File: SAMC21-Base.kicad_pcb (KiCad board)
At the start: 4 copper layers, 25.4 x 42.5 mm, 52 parts, among them J1 Conn_01x04, J2 Conn_01x10, J3 Conn_01x10, J5 Conn_ARM_JTAG_SWD_10, U1 ATSAMC21E18A-AUT, U2 TJA1043T, U3 TPS560430Y, U4 MCP1703A, Y1 ABM3-8.000MHZ-D2Y-T

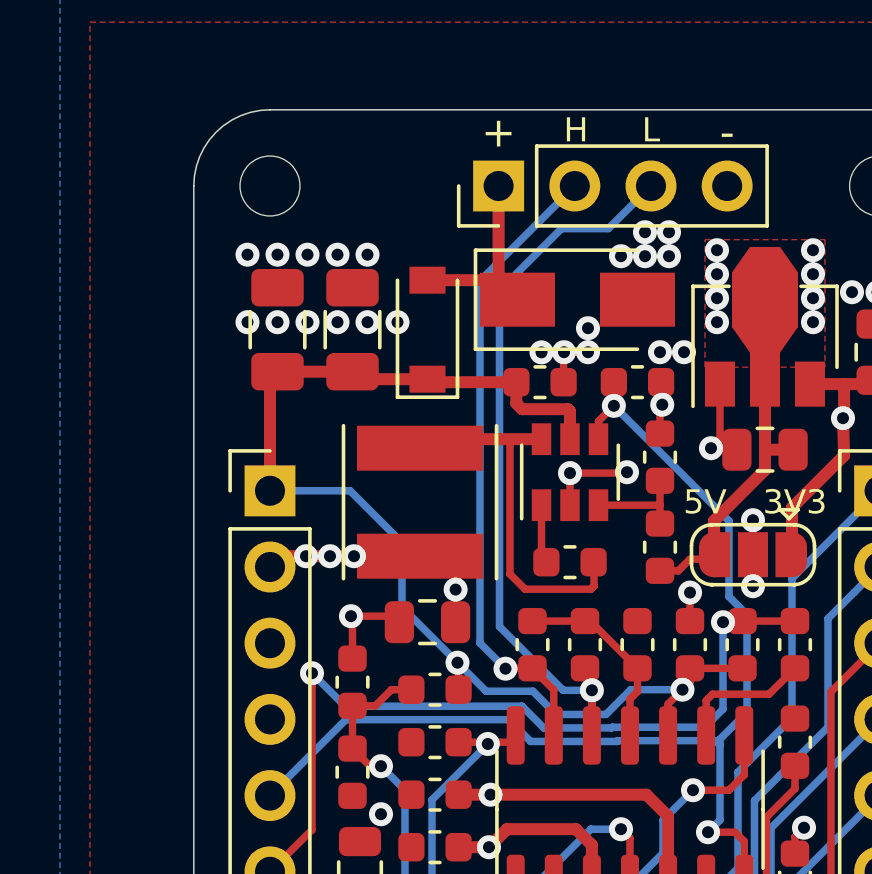
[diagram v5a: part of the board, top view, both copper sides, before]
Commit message: add various ESD, EMV and overcurrent protections
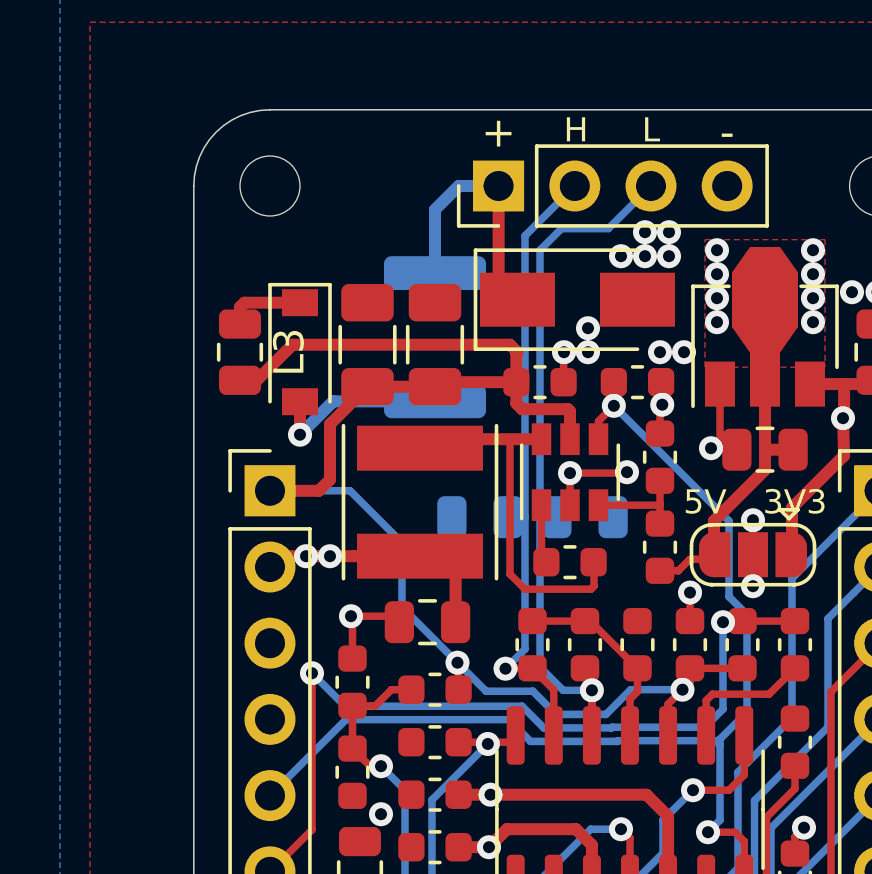
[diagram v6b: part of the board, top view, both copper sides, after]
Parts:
- added F1: 1812L020/60, Fuse:Fuse_1812_4532Metric, B.Cu at (107.1, 58.4)
- added L3: MLP2012V4R7MT0S1, Inductor_SMD:L_0805_2012Metric, F.Cu at (100.6, 58.9)
- added RV1: CT0805K25G, Resistor_SMD:R_0805_2012Metric, B.Cu at (108.6, 64.4)
- added RV2: CT0805K25G, Resistor_SMD:R_0805_2012Metric, B.Cu at (112.1, 64.4)
- moved D1 4.32 mm to (102.6, 58.9), turned to 270 degrees
- moved C20 3.04 mm to (104.8, 58.6)
- moved C1 2.80 mm to (107.1, 58.6)
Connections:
- D1 pad 1: +36V -> Net-(D1-Pad1)
- D1 pad 2: VBUS -> Net-(D1-Pad2)
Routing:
- net +36V: track 39.4 -> 48.8 mm
- net Net-(D1-Pad2): track 0.00 -> 6.06 mm, vias 0 -> 1
- net Net-(D1-Pad1): track 0.00 -> 2.62 mm
- net VBUS: track 5.54 -> 7.72 mm
- net GND: track 30.5 -> 29.8 mm, vias 40 -> 28
- net CAN_L: track 25.5 -> 24.9 mm
- net +5V: track 44.2 -> 44.0 mm, vias 13 -> 11

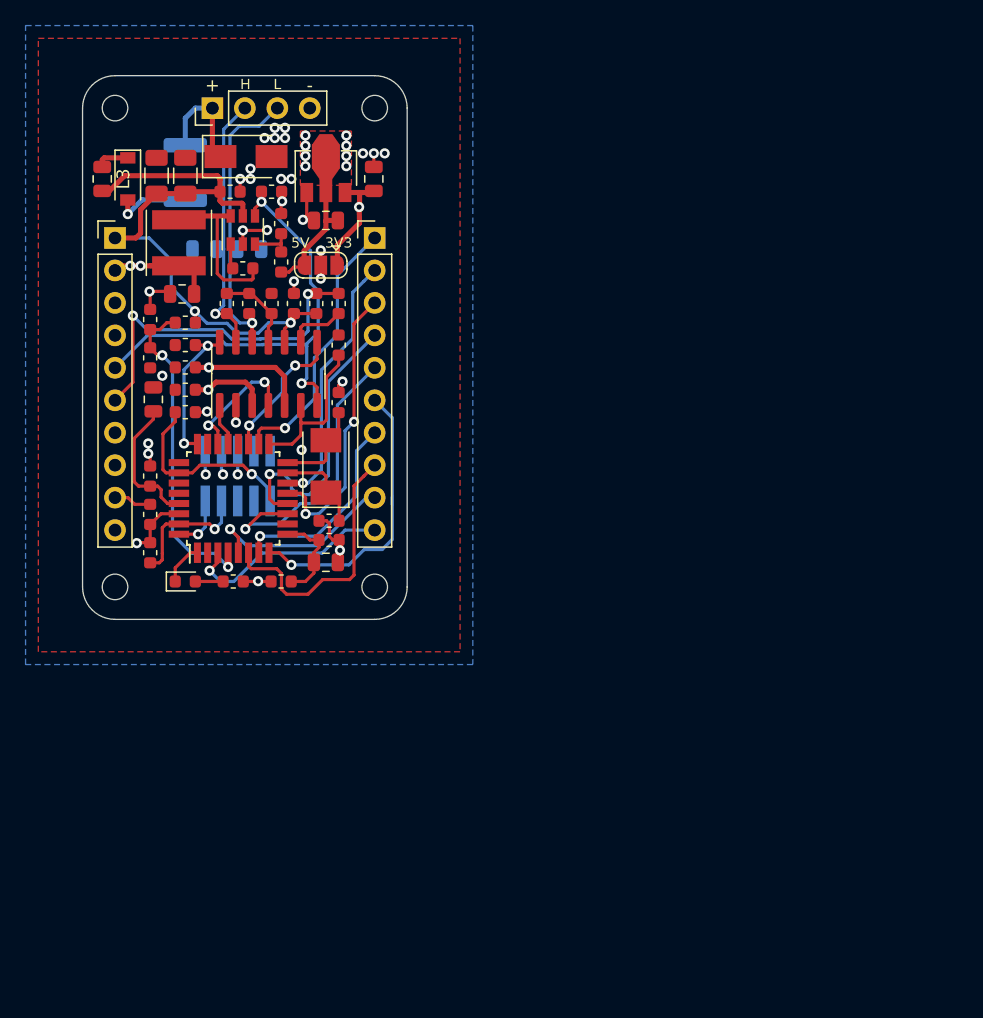
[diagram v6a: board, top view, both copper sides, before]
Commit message: redo layout. from scratch.
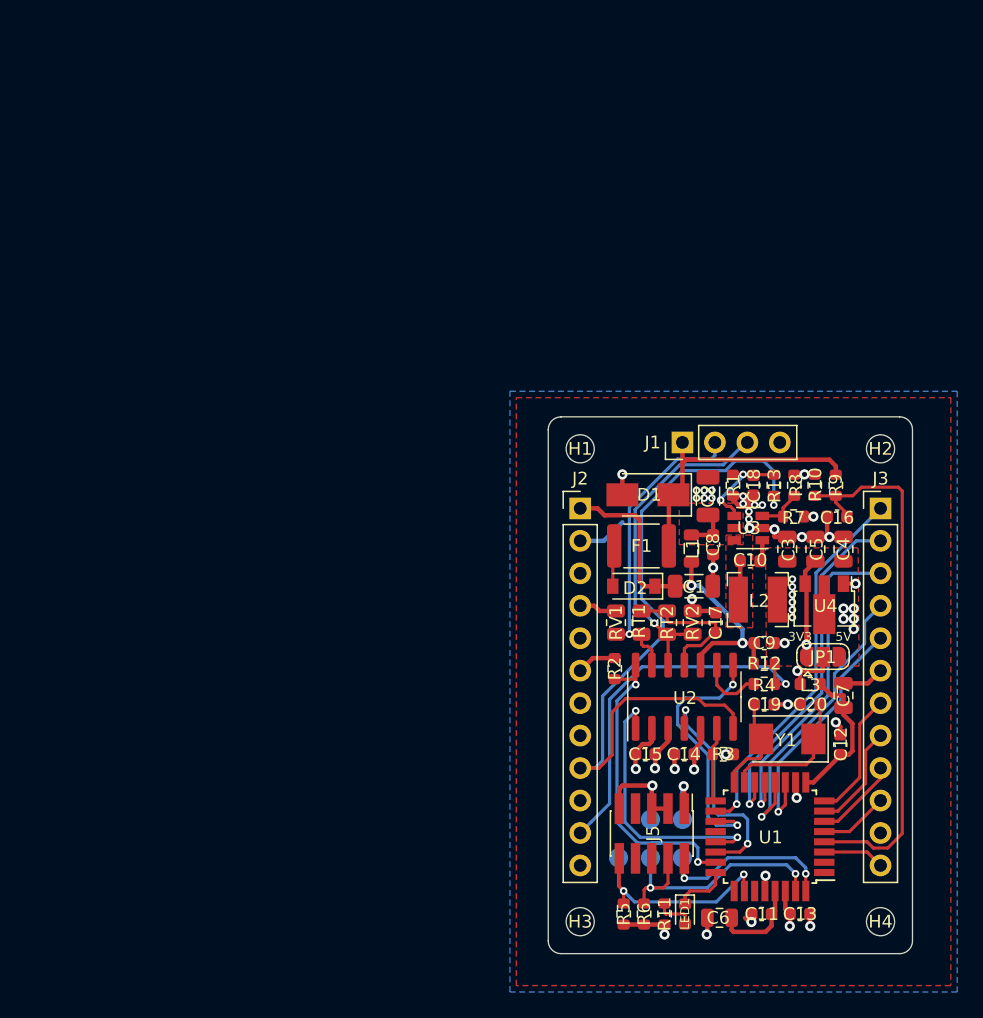
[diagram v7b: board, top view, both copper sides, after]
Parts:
- removed D3: SMAJ40A, Diode_SMD:D_SMA
- added C4: 10uF/10V, Capacitor_SMD:C_0805_2012Metric, F.Cu at (158.6, 87.8)
- added LED1: LED_Small, LED_SMD:LED_0603_1608Metric, F.Cu at (146.2, 116.4)
- added R13: 100K, Resistor_SMD:R_0603_1608Metric, F.Cu at (153.2, 82.8)
- added TP1: TestPoint, TestPoint:TestPoint_Pad_D1.5mm, B.Cu at (141.0, 112.0)
- added TP2: TestPoint, TestPoint:TestPoint_Pad_D1.5mm, B.Cu at (143.5, 112.0)
- added TP3: TestPoint, TestPoint:TestPoint_Pad_D1.5mm, B.Cu at (146.0, 112.0)
- added TP4: TestPoint, TestPoint:TestPoint_Pad_D1.5mm, B.Cu at (146.0, 109.0)
- added TP5: TestPoint, TestPoint:TestPoint_Pad_D1.5mm, B.Cu at (143.5, 109.0)
- C1: value 10uF/50V -> 4.7uF/50V
- C16: value 100nF/50V -> 100nF
- C18: value 18pF -> 2.2nF
- C2: value 100nF/100V -> 4.7uF/50V; footprint Capacitor_SMD:C_0603_1608Metric -> Capacitor_SMD:C_1206_3216Metric
- C20: value 10uF/50V -> 18pF; footprint Capacitor_SMD:C_1206_3216Metric -> Capacitor_SMD:C_0603_1608Metric
- C3, C5, C6, C7: value 10uF -> 10uF/10V
- C8: value 10uF -> 100nF/100V; footprint Capacitor_SMD:C_0805_2012Metric -> Capacitor_SMD:C_0603_1608Metric
- C9: value 100nF -> 100nF/100V
- D1: value MBR0560 -> 36V; footprint Diode_SMD:D_SOD-123 -> Diode_SMD:D_SMA
- D2: value LED_Small -> 60V 1A; footprint LED_SMD:LED_0603_1608Metric -> Diode_SMD:D_SOD-123
- F1: value 1812L020/60 -> 60V 200mA; moved to F.Cu
- H1, H2, H3, H4: footprint MountingHole:MountingHole_2mm -> MountingHole:MountingHole_2.2mm_M2
- J2, J3: footprint Connector_PinHeader_2.54mm:PinHeader_1x10_P2.54mm_Vertical -> Connector_PinHeader_2.54mm:PinHeader_1x12_P2.54mm_Vertical
- J5: moved to F.Cu
- L1: value NR5040T100M -> 4.7uH; footprint Inductor_SMD:L_Taiyo-Yuden_NR-50xx -> Inductor_SMD:L_0805_2012Metric
- L2: value MPZ1608S221A -> 10uH; footprint Inductor_SMD:L_0603_1608Metric -> Inductor_SMD:L_Bourns-SRN4018
- L3: value MLP2012V4R7MT0S1 -> 220R@100MHz; footprint Inductor_SMD:L_0805_2012Metric -> Inductor_SMD:L_0603_1608Metric
- R1: value 100K -> 15K
- R10: value 10K -> 6K8
- RT1, RT2: footprint Resistor_SMD:R_0603_1608Metric -> Resistor_SMD:R_0805_2012Metric
- RV1, RV2: value CT0805K25G -> 25V; moved to F.Cu
- U3: value TPS560430Y -> LMR50410-Q1
- Y1: value ABM3-8.000MHZ-D2Y-T -> 8MHz
- moved L3 68.1 mm to (156.0, 98.4), turned to 180 degrees
- moved C20 65.8 mm to (156.0, 100.0), turned to 0 degrees
- moved H3 65.7 mm to (138.0, 117.0)
- moved C6 63.8 mm to (148.9, 116.7), turned to 180 degrees
- moved H2 60.9 mm to (161.5, 80.0)
- moved C13 59.7 mm to (155.2, 116.4), turned to 0 degrees
- moved C11 58.9 mm to (152.2, 116.4), turned to 180 degrees
- moved C7 58.8 mm to (158.6, 99.3)
- moved R10 53.6 mm to (156.3, 82.8)
- moved C9 53.0 mm to (152.4, 95.2), turned to 0 degrees
- moved R9 52.5 mm to (158.0, 82.8), turned to 270 degrees
- moved R5 52.1 mm to (141.4, 116.4), turned to 90 degrees
- moved U4 51.6 mm to (157.1, 92.2), turned to 270 degrees
- moved C3 51.4 mm to (154.2, 87.8), turned to 90 degrees
- moved C1 51.1 mm to (146.9, 90.8), turned to 0 degrees
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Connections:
- net Net-(C10-Pad2) renamed /CB
- net Net-(R7-Pad2) renamed /FB
- C10 pad 1: Net-(C10-Pad1) -> /SW
- C16 pad 1: +36V -> /VBUS_ADC
- C18 pad 1: GND -> /EN
- C18 pad 2: Net-(C18-Pad2) -> GND
- C2 pad 1: +36V -> /DCDC_IN
- C20 pad 1: +36V -> GND
- C20 pad 2: GND -> Net-(C20-Pad2)
- C5 pad 1: +5V -> +3V3
- C6 pad 1: +3V3 -> /VDDCORE
- C7 pad 1: /VDDCORE -> /VDDANA
- C8 pad 1: /VDDANA -> /DCDC_IN
- C9 pad 1: /VBUS_ADC -> +36V
- D1 pad 1: Net-(D1-Pad1) -> VBUS
- D1 pad 2: Net-(D1-Pad2) -> GND
- D2 pad 1: Net-(D2-Pad1) -> +36V
- F1 pad 1: Net-(D1-Pad2) -> Net-(D2-Pad2)
- J2 pad 2: +5V -> GND
- J2 pad 3: +3V3 -> +5V
- J2 pad 4: VDD -> GND
- J2 pad 5: INH -> +3V3
- J2 pad 6: WAKE -> GND
- J2 pad 7: GND -> VDD
- J2 pad 9: GND -> INH
- J3 pad 10: PA02 -> PA04
- J3 pad 6: PA07 -> GND
- J3 pad 7: PA06 -> PA07
- J3 pad 8: PA05 -> PA06
- J3 pad 9: PA04 -> PA05
- L1 pad 1: Net-(C10-Pad1) -> +36V
- L1 pad 2: +5V -> /DCDC_IN
- L2 pad 1: /VDDANA -> /SW
- L2 pad 2: VDD -> +5V
- L3 pad 1: Net-(D1-Pad1) -> /VDDANA
- L3 pad 2: +36V -> VDD
- R1 pad 1: INH -> /EN
- R11 pad 2: Net-(D2-Pad2) -> Net-(LED1-Pad2)
- R9 pad 1: +36V -> VBUS
- RV2 pad 1: CAN_L -> GND
- RV2 pad 2: GND -> CAN_L
- U1 pad 1: Net-(D2-Pad1) -> Net-(U1-Pad1)
- U1 pad 15: Net-(C19-Pad2) -> Net-(C20-Pad2)
- U1 pad 16: Net-(C18-Pad2) -> Net-(C19-Pad2)
- U1 pad 23: Net-(U1-Pad23) -> CAN_STB
- U1 pad 24: CAN_STB -> LED
- U3 pad 4: INH -> /EN
- U3 pad 5: +36V -> /DCDC_IN
- U3 pad 6: Net-(C10-Pad1) -> /SW
- Y1 pad 1: Net-(C19-Pad2) -> Net-(C20-Pad2)
- Y1 pad 2: Net-(C18-Pad2) -> Net-(C19-Pad2)
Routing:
- net GND: track 29.8 -> 65.0 mm, vias 28 -> 33
- net INH: track 37.9 -> 57.7 mm, vias 2 -> 1
- net +36V: track 48.8 -> 29.5 mm
- net CAN_TX: track 3.30 -> 21.6 mm, vias 0 -> 2
- net +5V: track 44.0 -> 25.9 mm, vias 11 -> 13
- net /VBUS_ADC: track 25.7 -> 42.8 mm, vias 2 -> 0
- net Net-(C10-Pad1): track 16.3 -> 0.00 mm
- net CAN_STB: track 11.5 -> 26.0 mm
- net PA05: track 20.8 -> 6.61 mm
- net VBUS: track 7.72 -> 21.5 mm
- net PA07: track 22.9 -> 10.0 mm, vias 1 -> 0
- net PA02: track 16.6 -> 4.83 mm, vias 1 -> 0
- net SWDIO: track 4.33 -> 15.5 mm, vias 1 -> 2
- net Net-(C20-Pad2): track 0.00 -> 11.1 mm
- net VDD: track 30.0 -> 19.0 mm, vias 7 -> 5
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- added copper zone on F.Cu, net /DCDC_IN
- added copper zone on F.Cu, net /SW
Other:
- board size 25.4 x 42.5 mm -> 28.5 x 42 mm
- net class Default: via_dia 0.8 -> 0.6; via_drill 0.4 -> 0.3
- net class Power: trace_width 0.4 -> 0.35
- rule via_min_drill: 0.3 -> 0.2
- board text removed: "+"
- board text removed: "-"
- board text removed: "H"
- board text removed: "L"
- board text removed: "SAMC21 Base v0.1 xor@xor.wtf"

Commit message: minor cleanups
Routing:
- net Net-(C19-Pad2): track 7.75 -> 11.5 mm
- net PA09: track 23.5 -> 20.6 mm
- net PA08: track 19.4 -> 17.7 mm
- net /VDDANA: track 11.5 -> 12.2 mm
